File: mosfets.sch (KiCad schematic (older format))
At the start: 28 parts, among them Q12 PSMN1R2-30YLC,115, Q13 PSMN1R2-30YLC,115, Q14 PSMN1R2-30YLC,115, Q15 PMPB11EN, Q16 PMPB11EN, Q17 PMPB11EN, Q18 PMPB11EN

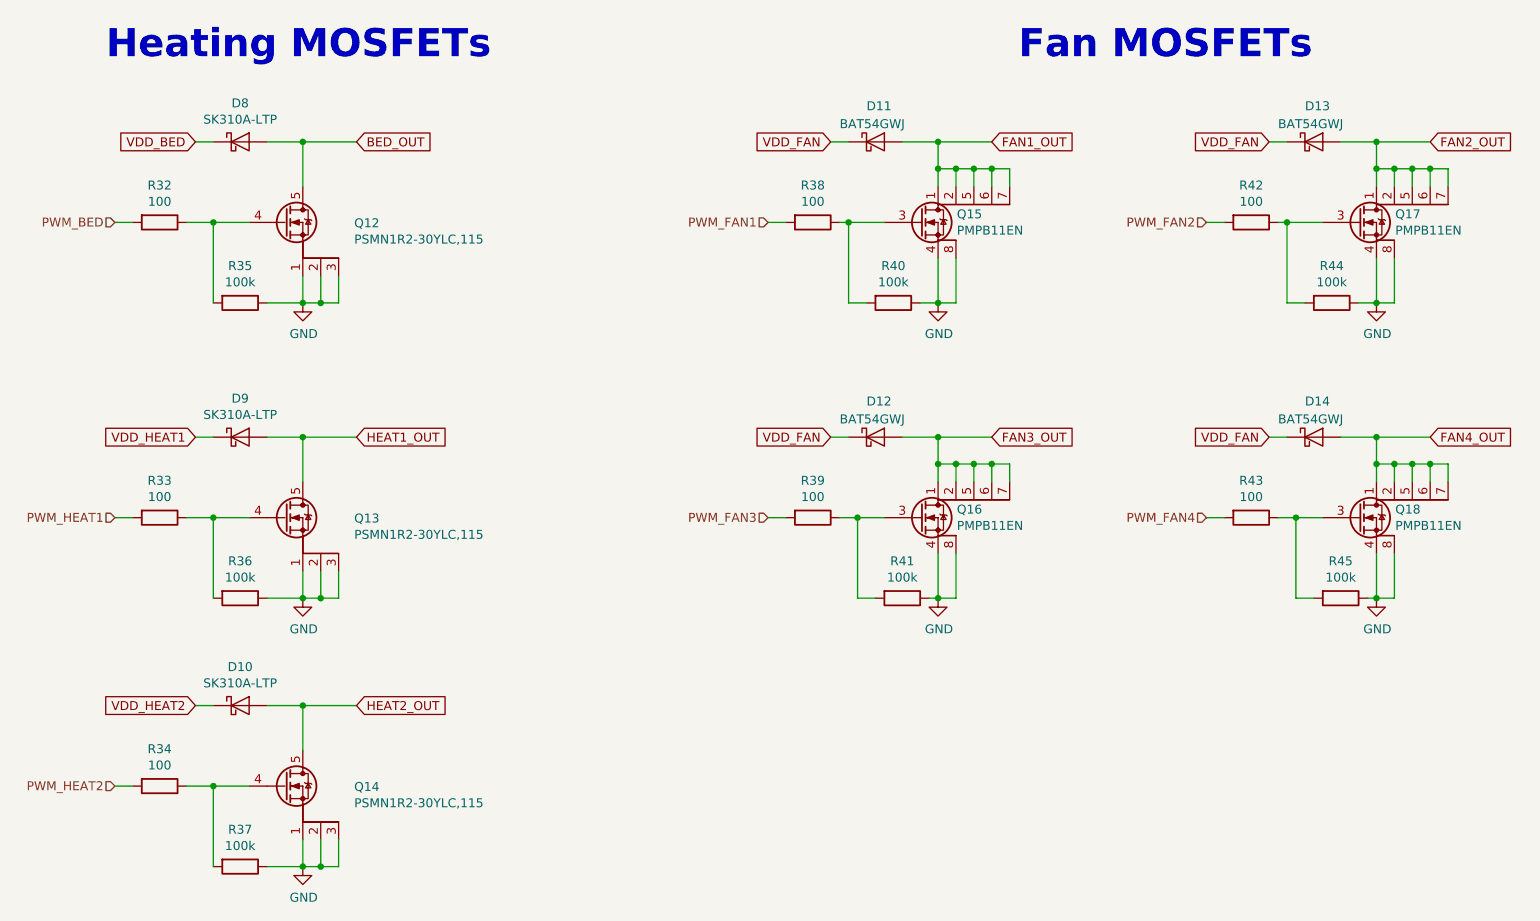
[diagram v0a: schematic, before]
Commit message: Updated board to version 1.2
 * Switched small MOSFETs to SOT-23 package
 * Redesigned TMC*160 driver layout
 * Changed 01x03 to 02x03 jumper for FAN voltage selection
 * Switches STATUS_LED pin
 * Some copper pour optimizations
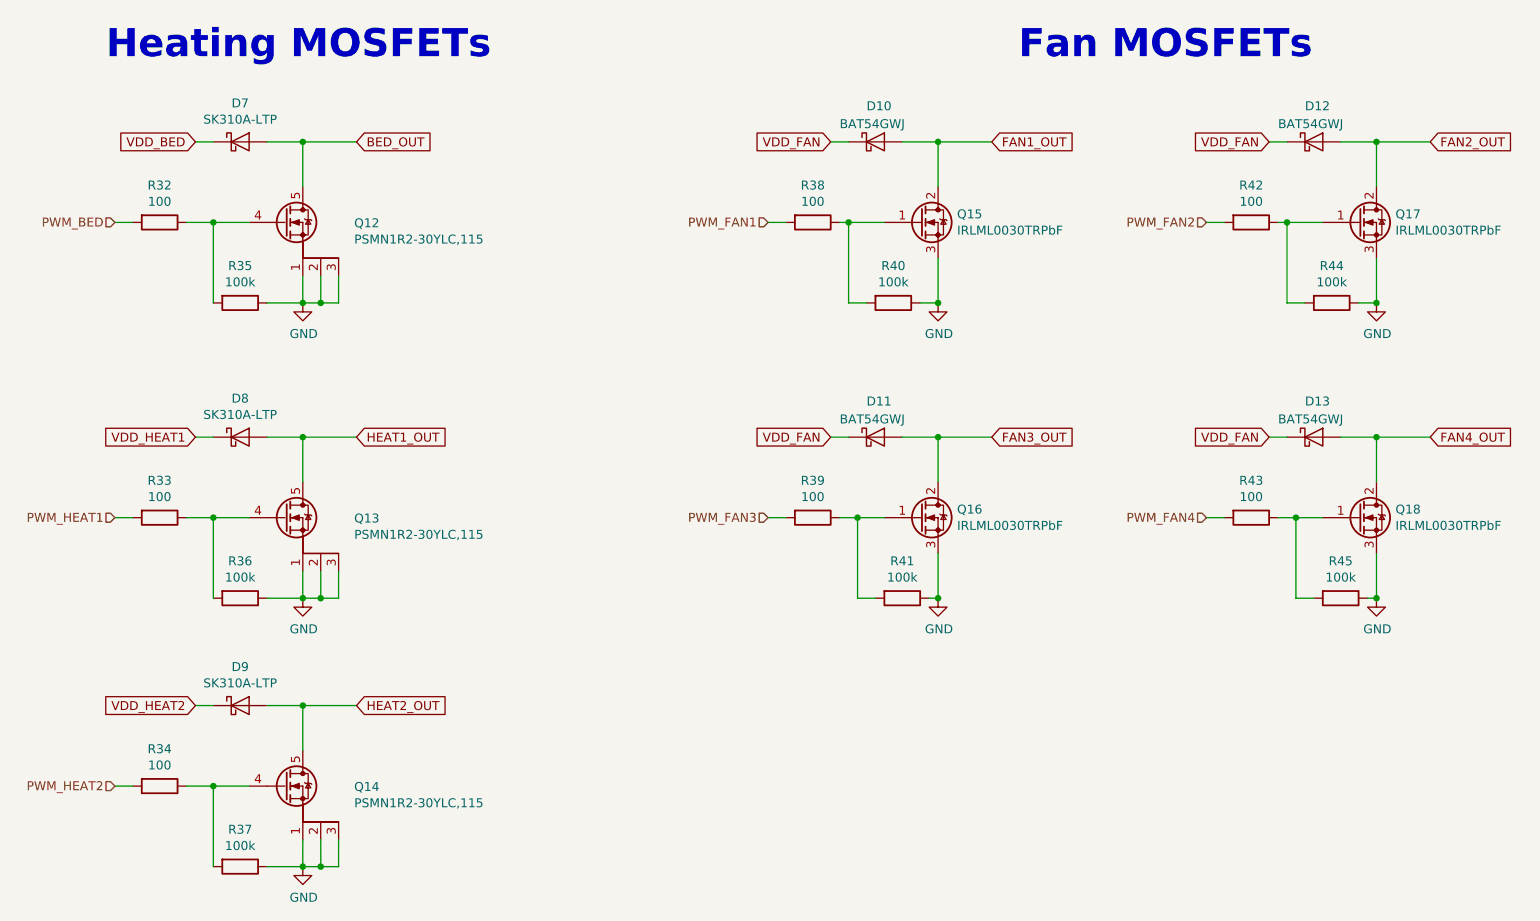
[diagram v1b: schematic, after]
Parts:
- removed Q15, Q16, Q17, Q18: PMPB11EN, heteromycin:SOT1220, symbol heteromycin:PMPB20EN
- added Q15, Q16, Q17, Q18: IRLML0030TRPbF, Package_TO_SOT_SMD:SOT-23, symbol Device:Q_NMOS_GDS
- renumbered D11 to D10, D12 to D11, D13 to D12, D14 to D13, D8 to D7, D9 to D8, D10 to D9
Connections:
- net FAN1_OUT: now also Q15.2 (D)
- net FAN2_OUT: now also Q17.2 (D)
- net FAN3_OUT: now also Q16.2 (D)
- net FAN4_OUT: now also Q18.2 (D)
- net GND: now also Q15.3 (S), Q16.3 (S), Q17.3 (S), Q18.3 (S)
- net at R38.1, R40.2: now also Q15.1 (G)
- net at R39.1, R41.2: now also Q16.1 (G)
- net at R42.1, R44.2: now also Q17.1 (G)
- net at R43.1, R45.2: now also Q18.1 (G)
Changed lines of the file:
@@
 $EndDescr
 $Comp
-L Device:D_Schottky D8
+L Device:D_Schottky D7
 U 1 1 5B1A3271
 P 1950 1300
-F 0 "D8" H 1950 1516 50  0000 C CNN
+F 0 "D7" H 1950 1516 50  0000 C CNN
 F 1 "SK310A-LTP" H 1950 1425 50  0000 C CNN
 F 2 "Diode_SMD:D_SMA" H 1950 1300 50  0001 C CNN
@@
 	2300 1550 2300 1300
 $Comp
-L Device:D_Schottky D9
+L Device:D_Schottky D8
 U 1 1 5B1B03B6
 P 1950 2950
-F 0 "D9" H 1950 3166 50  0000 C CNN
+F 0 "D8" H 1950 3166 50  0000 C CNN
 F 1 "SK310A-LTP" H 1950 3075 50  0000 C CNN
 F 2 "Diode_SMD:D_SMA" H 1950 2950 50  0001 C CNN
@@
 Connection ~ 2300 2950
 $Comp
-L heteromycin:PMPB20EN Q15
-U 1 1 5B1FB146
-P 5750 1750
-F 0 "Q15" H 5955 1796 50  0000 L CNN
-F 1 "PMPB11EN" H 5955 1705 50  0000 L CNN
-F 2 "heteromycin:SOT1220" H 5950 1675 50  0001 L CIN
-F 3 "https://assets.nexperia.com/documents/data-sheet/PMPB11EN.pdf" H 5750 1750 50  0001 L CNN
-	1    5750 1750
-	1    0    0    -1
-$EndComp
-$Comp
 L Device:R R38
 U 1 1 5B1FB287
@@
 	5250 1300 5350 1300
 Wire Wire Line
-	5850 1550 5850 1450
-Wire Wire Line
 	5650 1300 5850 1300
 Connection ~ 5850 1300
@@
 	5250 2950 5350 2950
 Wire Wire Line
-	5850 3200 5850 3100
-Wire Wire Line
 	5650 2950 5850 2950
 Connection ~ 5850 2950
@@
 $EndComp
 $Comp
-L Device:D_Schottky D11
+L Device:D_Schottky D10
 U 1 1 5BD6B250
 P 5500 1300
-F 0 "D11" H 5450 1500 50  0000 L CNN
+F 0 "D10" H 5450 1500 50  0000 L CNN
 F 1 "BAT54GWJ" H 5300 1400 50  0000 L CNN
 F 2 "Diode_SMD:D_SOD-123" H 5500 1300 50  0001 C CNN
@@
 $EndComp
 $Comp
-L Device:D_Schottky D12
+L Device:D_Schottky D11
 U 1 1 5BD6D4A2
 P 5500 2950
-F 0 "D12" H 5450 3150 50  0000 L CNN
+F 0 "D11" H 5450 3150 50  0000 L CNN
 F 1 "BAT54GWJ" H 5300 3050 50  0000 L CNN
 F 2 "Diode_SMD:D_SOD-123" H 5500 2950 50  0001 C CNN
@@
 	1    0    0    -1
 $EndComp
-$Comp
-L heteromycin:PMPB20EN Q16
-U 1 1 5BC35639
-P 5750 3400
-F 0 "Q16" H 5955 3446 50  0000 L CNN
-F 1 "PMPB11EN" H 5955 3355 50  0000 L CNN
-F 2 "heteromycin:SOT1220" H 5950 3325 50  0001 L CIN
-F 3 "https://assets.nexperia.com/documents/data-sheet/PMPB11EN.pdf" H 5750 3400 50  0001 L CNN
-	1    5750 3400
-	1    0    0    -1
-$EndComp
-Wire Wire Line
-	6250 3200 6250 3100
-Wire Wire Line
-	6250 3100 6150 3100
-Connection ~ 5850 3100
-Wire Wire Line
-	5850 3100 5850 2950
-Wire Wire Line
-	5950 3100 5950 3200
-Connection ~ 5950 3100
-Wire Wire Line
-	5950 3100 5850 3100
-Wire Wire Line
-	6050 3100 6050 3200
-Connection ~ 6050 3100
-Wire Wire Line
-	6050 3100 5950 3100
-Wire Wire Line
-	6150 3100 6150 3200
-Connection ~ 6150 3100
-Wire Wire Line
-	6150 3100 6050 3100
-Wire Wire Line
-	5950 3600 5950 3850
-Wire Wire Line
-	5950 3850 5850 3850
-Wire Wire Line
-	5850 2200 5950 2200
-Wire Wire Line
-	5950 2200 5950 1950
-Wire Wire Line
-	5950 1550 5950 1450
-Wire Wire Line
-	5950 1450 5850 1450
-Connection ~ 5850 1450
-Wire Wire Line
-	5850 1450 5850 1300
-Wire Wire Line
-	5950 1450 6050 1450
-Wire Wire Line
-	6250 1450 6250 1550
-Connection ~ 5950 1450
-Wire Wire Line
-	6150 1550 6150 1450
-Connection ~ 6150 1450
-Wire Wire Line
-	6150 1450 6250 1450
-Wire Wire Line
-	6050 1550 6050 1450
-Connection ~ 6050 1450
-Wire Wire Line
-	6050 1450 6150 1450
 Text Notes 6300 850  0    157  ~ 31
 Fan MOSFETs
@@
 PWM_HEAT2
 $Comp
-L Device:D_Schottky D10
+L Device:D_Schottky D9
 U 1 1 5BC4CDE5
 P 1950 4450
-F 0 "D10" H 1950 4666 50  0000 C CNN
+F 0 "D9" H 1950 4666 50  0000 C CNN
 F 1 "SK310A-LTP" H 1950 4575 50  0000 C CNN
 F 2 "Diode_SMD:D_SMA" H 1950 4450 50  0001 C CNN
@@
 $EndComp
 $Comp
-L heteromycin:PMPB20EN Q17
-U 1 1 5BC57CCA
-P 8200 1750
-F 0 "Q17" H 8405 1796 50  0000 L CNN
-F 1 "PMPB11EN" H 8405 1705 50  0000 L CNN
-F 2 "heteromycin:SOT1220" H 8400 1675 50  0001 L CIN
-F 3 "https://assets.nexperia.com/documents/data-sheet/PMPB11EN.pdf" H 8200 1750 50  0001 L CNN
-	1    8200 1750
-	1    0    0    -1
-$EndComp
-$Comp
 L Device:R R42
 U 1 1 5BC57CD1
@@
 	7700 1300 7800 1300
 Wire Wire Line
-	8300 1550 8300 1450
-Wire Wire Line
 	8100 1300 8300 1300
 Connection ~ 8300 1300
@@
 	7700 2950 7800 2950
 Wire Wire Line
-	8300 3200 8300 3100
-Wire Wire Line
 	8100 2950 8300 2950
 Connection ~ 8300 2950
@@
 VDD_FAN
 $Comp
-L Device:D_Schottky D13
+L Device:D_Schottky D12
 U 1 1 5BC57D0F
 P 7950 1300
-F 0 "D13" H 7900 1500 50  0000 L CNN
+F 0 "D12" H 7900 1500 50  0000 L CNN
 F 1 "BAT54GWJ" H 7750 1400 50  0000 L CNN
 F 2 "Diode_SMD:D_SOD-123" H 7950 1300 50  0001 C CNN
@@
 $EndComp
 $Comp
-L Device:D_Schottky D14
+L Device:D_Schottky D13
 U 1 1 5BC57D16
 P 7950 2950
-F 0 "D14" H 7900 3150 50  0000 L CNN
+F 0 "D13" H 7900 3150 50  0000 L CNN
 F 1 "BAT54GWJ" H 7750 3050 50  0000 L CNN
 F 2 "Diode_SMD:D_SOD-123" H 7950 2950 50  0001 C CNN
@@
 	1    0    0    -1
 $EndComp
-$Comp
-L heteromycin:PMPB20EN Q18
-U 1 1 5BC57D1D
-P 8200 3400
-F 0 "Q18" H 8405 3446 50  0000 L CNN
-F 1 "PMPB11EN" H 8405 3355 50  0000 L CNN
-F 2 "heteromycin:SOT1220" H 8400 3325 50  0001 L CIN
-F 3 "https://assets.nexperia.com/documents/data-sheet/PMPB11EN.pdf" H 8200 3400 50  0001 L CNN
-	1    8200 3400
-	1    0    0    -1
-$EndComp
-Wire Wire Line
-	8700 3200 8700 3100
-Wire Wire Line
-	8700 3100 8600 3100
-Connection ~ 8300 3100
-Wire Wire Line
-	8300 3100 8300 2950
-Wire Wire Line
-	8400 3100 8400 3200
-Connection ~ 8400 3100
-Wire Wire Line
-	8400 3100 8300 3100
-Wire Wire Line
-	8500 3100 8500 3200
-Connection ~ 8500 3100
-Wire Wire Line
-	8500 3100 8400 3100
-Wire Wire Line
-	8600 3100 8600 3200
-Connection ~ 8600 3100
-Wire Wire Line
-	8600 3100 8500 3100
-Wire Wire Line
-	8400 3600 8400 3850
-Wire Wire Line
-	8400 3850 8300 3850
-Wire Wire Line
-	8300 2200 8400 2200
-Wire Wire Line
-	8400 2200 8400 1950
-Wire Wire Line
-	8400 1550 8400 1450
-Wire Wire Line
-	8400 1450 8300 1450
-Connection ~ 8300 1450
-Wire Wire Line
-	8300 1450 8300 1300
-Wire Wire Line
-	8400 1450 8500 1450
-Wire Wire Line
-	8700 1450 8700 1550
-Connection ~ 8400 1450
-Wire Wire Line
-	8600 1550 8600 1450
-Connection ~ 8600 1450
-Wire Wire Line
-	8600 1450 8700 1450
-Wire Wire Line
-	8500 1550 8500 1450
-Connection ~ 8500 1450
-Wire Wire Line
-	8500 1450 8600 1450
 $Comp
 L power:GND #PWR065
@@
 Text GLabel 8600 2950 2    50   Input ~ 0
 FAN4_OUT
+$Comp
+L Device:Q_NMOS_GDS Q?
+U 1 1 5BFEEB5C
+P 5750 1750
+AR Path="/5BC77F8A/5BFEEB5C" Ref="Q?"  Part="1"
+AR Path="/5BC2F52C/5BFEEB5C" Ref="Q?"  Part="1"
+AR Path="/5BC77BE8/5BFEEB5C" Ref="Q?"  Part="1"
+AR Path="/5BC77F87/5BFEEB5C" Ref="Q?"  Part="1"
+AR Path="/5BC77F8D/5BFEEB5C" Ref="Q?"  Part="1"
+AR Path="/5BC2F648/5BFEEB5C" Ref="Q15"  Part="1"
+F 0 "Q15" H 5956 1796 50  0000 L CNN
+F 1 "IRLML0030TRPbF" H 5956 1705 50  0000 L CNN
+F 2 "Package_TO_SOT_SMD:SOT-23" H 5950 1850 50  0001 C CNN
+F 3 "https://www.infineon.com/dgdl/irlml0030pbf.pdf?fileId=5546d462533600a401535664773825df" H 5750 1750 50  0001 C CNN
+	1    5750 1750
+	1    0    0    -1
+$EndComp
+Wire Wire Line
+	5850 1300 5850 1550
+Wire Wire Line
+	8300 1300 8300 1550
+Wire Wire Line
+	8300 2950 8300 3200
+Wire Wire Line
+	5850 2950 5850 3200
+$Comp
+L Device:Q_NMOS_GDS Q?
+U 1 1 5C004C12
+P 5750 3400
+AR Path="/5BC77F8A/5C004C12" Ref="Q?"  Part="1"
+AR Path="/5BC2F52C/5C004C12" Ref="Q?"  Part="1"
+AR Path="/5BC77BE8/5C004C12" Ref="Q?"  Part="1"
+AR Path="/5BC77F87/5C004C12" Ref="Q?"  Part="1"
+AR Path="/5BC77F8D/5C004C12" Ref="Q?"  Part="1"
+AR Path="/5BC2F648/5C004C12" Ref="Q16"  Part="1"
+F 0 "Q16" H 5956 3446 50  0000 L CNN
+F 1 "IRLML0030TRPbF" H 5956 3355 50  0000 L CNN
+F 2 "Package_TO_SOT_SMD:SOT-23" H 5950 3500 50  0001 C CNN
+F 3 "https://www.infineon.com/dgdl/irlml0030pbf.pdf?fileId=5546d462533600a401535664773825df" H 5750 3400 50  0001 C CNN
+	1    5750 3400
+	1    0    0    -1
+$EndComp
+$Comp
+L Device:Q_NMOS_GDS Q?
+U 1 1 5C006AFD
+P 8200 1750
+AR Path="/5BC77F8A/5C006AFD" Ref="Q?"  Part="1"
+AR Path="/5BC2F52C/5C006AFD" Ref="Q?"  Part="1"
+AR Path="/5BC77BE8/5C006AFD" Ref="Q?"  Part="1"
+AR Path="/5BC77F87/5C006AFD" Ref="Q?"  Part="1"
+AR Path="/5BC77F8D/5C006AFD" Ref="Q?"  Part="1"
+AR Path="/5BC2F648/5C006AFD" Ref="Q17"  Part="1"
+F 0 "Q17" H 8406 1796 50  0000 L CNN
+F 1 "IRLML0030TRPbF" H 8406 1705 50  0000 L CNN
+F 2 "Package_TO_SOT_SMD:SOT-23" H 8400 1850 50  0001 C CNN
+F 3 "https://www.infineon.com/dgdl/irlml0030pbf.pdf?fileId=5546d462533600a401535664773825df" H 8200 1750 50  0001 C CNN
+	1    8200 1750
+	1    0    0    -1
+$EndComp
+$Comp
+L Device:Q_NMOS_GDS Q?
+U 1 1 5C0089E5
+P 8200 3400
+AR Path="/5BC77F8A/5C0089E5" Ref="Q?"  Part="1"
+AR Path="/5BC2F52C/5C0089E5" Ref="Q?"  Part="1"
+AR Path="/5BC77BE8/5C0089E5" Ref="Q?"  Part="1"
+AR Path="/5BC77F87/5C0089E5" Ref="Q?"  Part="1"
+AR Path="/5BC77F8D/5C0089E5" Ref="Q?"  Part="1"
+AR Path="/5BC2F648/5C0089E5" Ref="Q18"  Part="1"
+F 0 "Q18" H 8406 3446 50  0000 L CNN
+F 1 "IRLML0030TRPbF" H 8406 3355 50  0000 L CNN
+F 2 "Package_TO_SOT_SMD:SOT-23" H 8400 3500 50  0001 C CNN
+F 3 "https://www.infineon.com/dgdl/irlml0030pbf.pdf?fileId=5546d462533600a401535664773825df" H 8200 3400 50  0001 C CNN
+	1    8200 3400
+	1    0    0    -1
+$EndComp
 $EndSCHEMATC
